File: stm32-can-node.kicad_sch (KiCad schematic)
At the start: 41 parts, among them J1 Conn_01x04_Pin, J2 Conn_01x10_Pin, J3 Conn_01x10_Pin, J4 Conn_01x05_Pin, U1 DS2484R_T, U2 R-783.3-0.5, U3 STM32U535CETx, U4 SN65HVD234, Y1 16MHz

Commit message: better pcb layout
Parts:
- added C16: 100n, Capacitor_SMD:C_0402_1005Metric, symbol Device:C
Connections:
- net +3.3V: now also C16.1
- net GND: now also C16.2
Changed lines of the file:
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@@
 	)
 	(junction
+		(at 156.21 157.48)
+		(diameter 0)
+		(color 0 0 0 0)
+	)
+	(junction
 		(at 232.41 26.67)
 		(diameter 0)
@@
 	(wire
 		(pts
+			(xy 68.58 33.02) (xy 68.58 36.83)
+		)
+		(stroke
+			(width 0)
+			(type default)
+		)
+	)
+	(wire
+		(pts
 			(xy 20.32 67.31) (xy 20.32 60.96)
 		)
@@
 	(wire
 		(pts
+			(xy 55.88 33.02) (xy 68.58 33.02)
+		)
+		(stroke
+			(width 0)
+			(type default)
+		)
+	)
+	(wire
+		(pts
 			(xy 68.58 44.45) (xy 68.58 46.99)
 		)
@@
 	(wire
 		(pts
-			(xy 55.88 33.02) (xy 68.58 33.02)
-		)
-		(stroke
-			(width 0)
-			(type default)
-		)
-	)
-	(wire
-		(pts
 			(xy 101.6 166.37) (xy 101.6 167.64)
 		)
@@
 	(wire
 		(pts
-			(xy 68.58 33.02) (xy 68.58 36.83)
+			(xy 68.58 25.4) (xy 68.58 33.02)
 		)
 		(stroke
@@
 	(wire
 		(pts
-			(xy 68.58 25.4) (xy 68.58 33.02)
-		)
-		(stroke
-			(width 0)
-			(type default)
-		)
-	)
-	(wire
-		(pts
 			(xy 247.65 59.69) (xy 254 59.69)
 		)
@@
 	)
 	(symbol
+		(lib_id "Device:C")
+		(at 156.21 161.29 0)
+		(unit 1)
+		(exclude_from_sim no)
+		(in_bom yes)
+		(on_board yes)
+		(dnp no)
+		(fields_autoplaced yes)
+		(property "Reference" "C16"
+			(at 160.02 160.02 0)
+			(effects
+				(font
+					(size 1.27 1.27)
+				)
+				(justify left)
+			)
+		)
+		(property "Value" "100n"
+			(at 160.02 162.56 0)
+			(effects
+				(font
+					(size 1.27 1.27)
+				)
+				(justify left)
+			)
+		)
+		(property "Footprint" "Capacitor_SMD:C_0402_1005Metric"
+			(at 157.1752 165.1 0)
+			(effects
+				(font
+					(size 1.27 1.27)
+				)
+				(hide yes)
+			)
+		)
+		(property "Datasheet" "~"
+			(at 156.21 161.29 0)
+			(effects
+				(font
+					(size 1.27 1.27)
+				)
+				(hide yes)
+			)
+		)
+		(property "Description" ""
+			(at 156.21 161.29 0)
+			(effects
+				(font
+					(size 1.27 1.27)
+				)
+			)
+		)
+		(pin "2"
+		)
+		(pin "1"
+		)
+		(instances
+			(project "stm32-can-node"
+				(path "/49496df6-b10b-410e-9292-bf7fa18df797"
+					(reference "C16")
+					(unit 1)
+				)
+			)
+		)
+	)
+	(symbol
 		(lib_name "+3.3V_2")
 		(lib_id "power:+3.3V")
@@
 					(unit 1)
 				)
+			)
+		)
+	)
+	(symbol
+		(lib_name "GND_1")
+		(lib_id "power:GND")
+		(at 156.21 165.1 0)
+		(unit 1)
+		(exclude_from_sim no)
+		(in_bom yes)
+		(on_board yes)
+		(dnp no)
+		(fields_autoplaced yes)
+		(property "Reference" "#PWR041"
+			(at 156.21 171.45 0)
+			(effects
+				(font
+					(size 1.27 1.27)
+				)
+				(hide yes)
+			)
+		)
+		(property "Value" "GND"
+			(at 156.21 170.18 0)
+			(effects
+				(font
+					(size 1.27 1.27)
+				)
+			)
+		)
+		(property "Footprint" ""
+			(at 156.21 165.1 0)
+			(effects
+				(font
+					(size 1.27 1.27)
+				)
+				(hide yes)
+			)
+		)
+		(property "Datasheet" ""
+			(at 156.21 165.1 0)
+			(effects
+				(font
+					(size 1.27 1.27)
+				)
+				(hide yes)
+			)
+		)
+		(property "Description" "Power symbol creates a global label with name \"GND\" , ground"
+			(at 156.21 165.1 0)
+			(effects
+				(font
+					(size 1.27 1.27)
+				)
+				(hide yes)
+			)
+		)
+		(pin "1"
+		)
+		(instances
+			(project "stm32-can-node"
+				(path "/49496df6-b10b-410e-9292-bf7fa18df797"
+					(reference "#PWR041")
+					(unit 1)
+				)

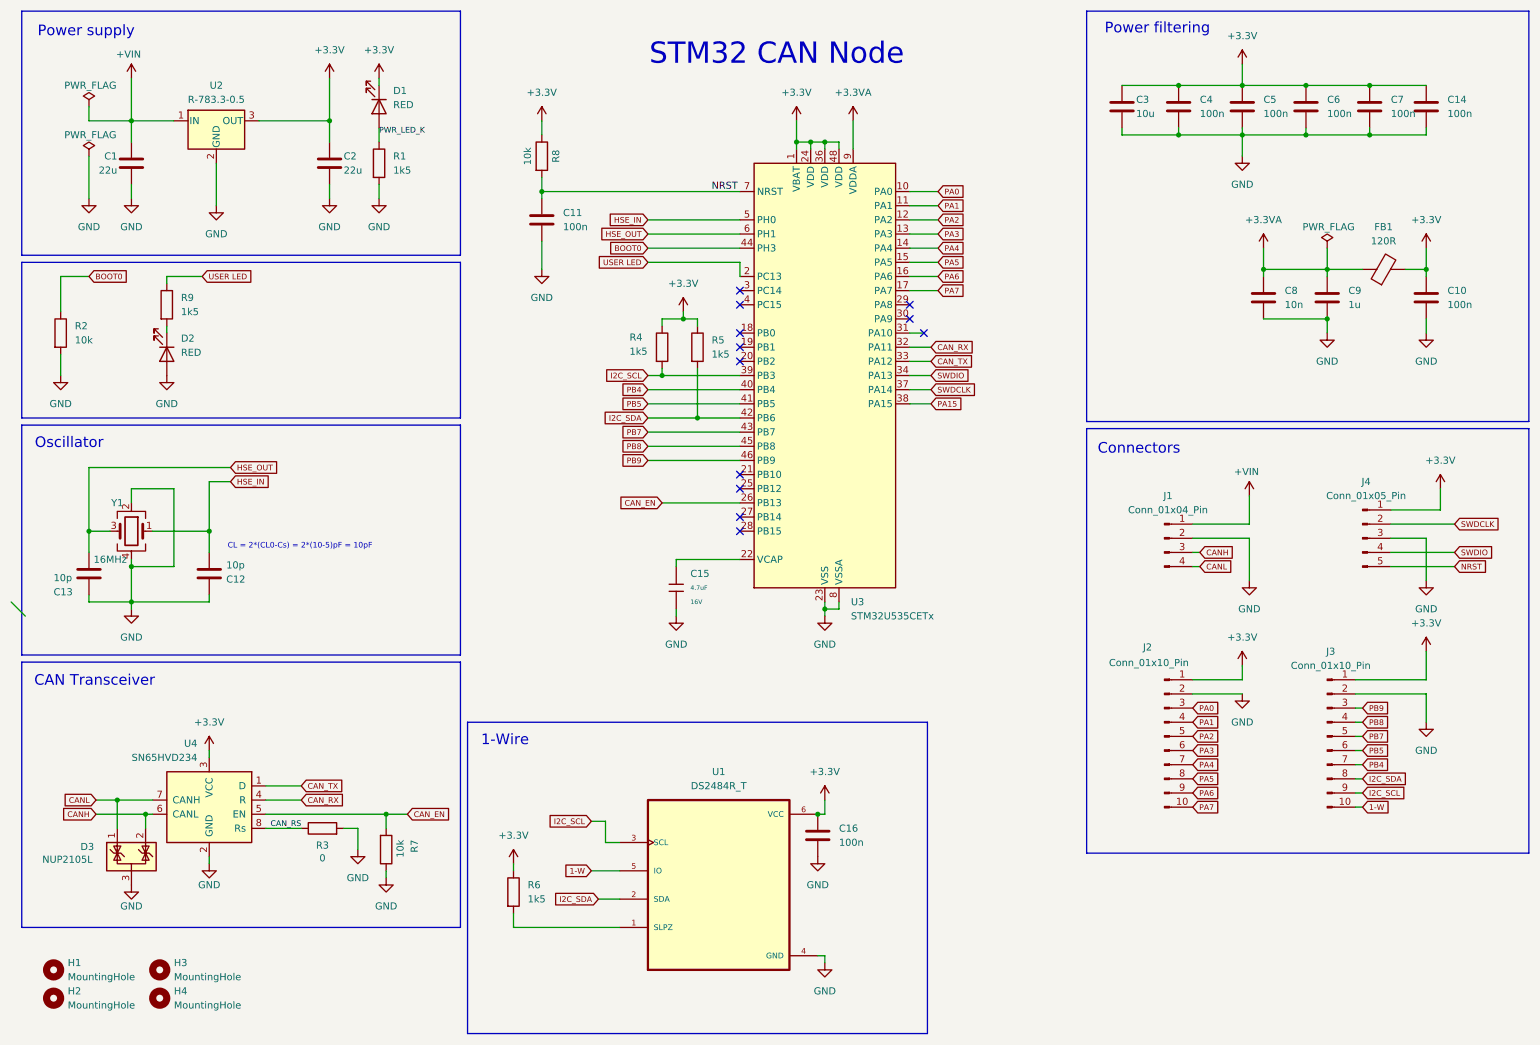
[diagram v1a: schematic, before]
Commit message: change to 11-pin connectors
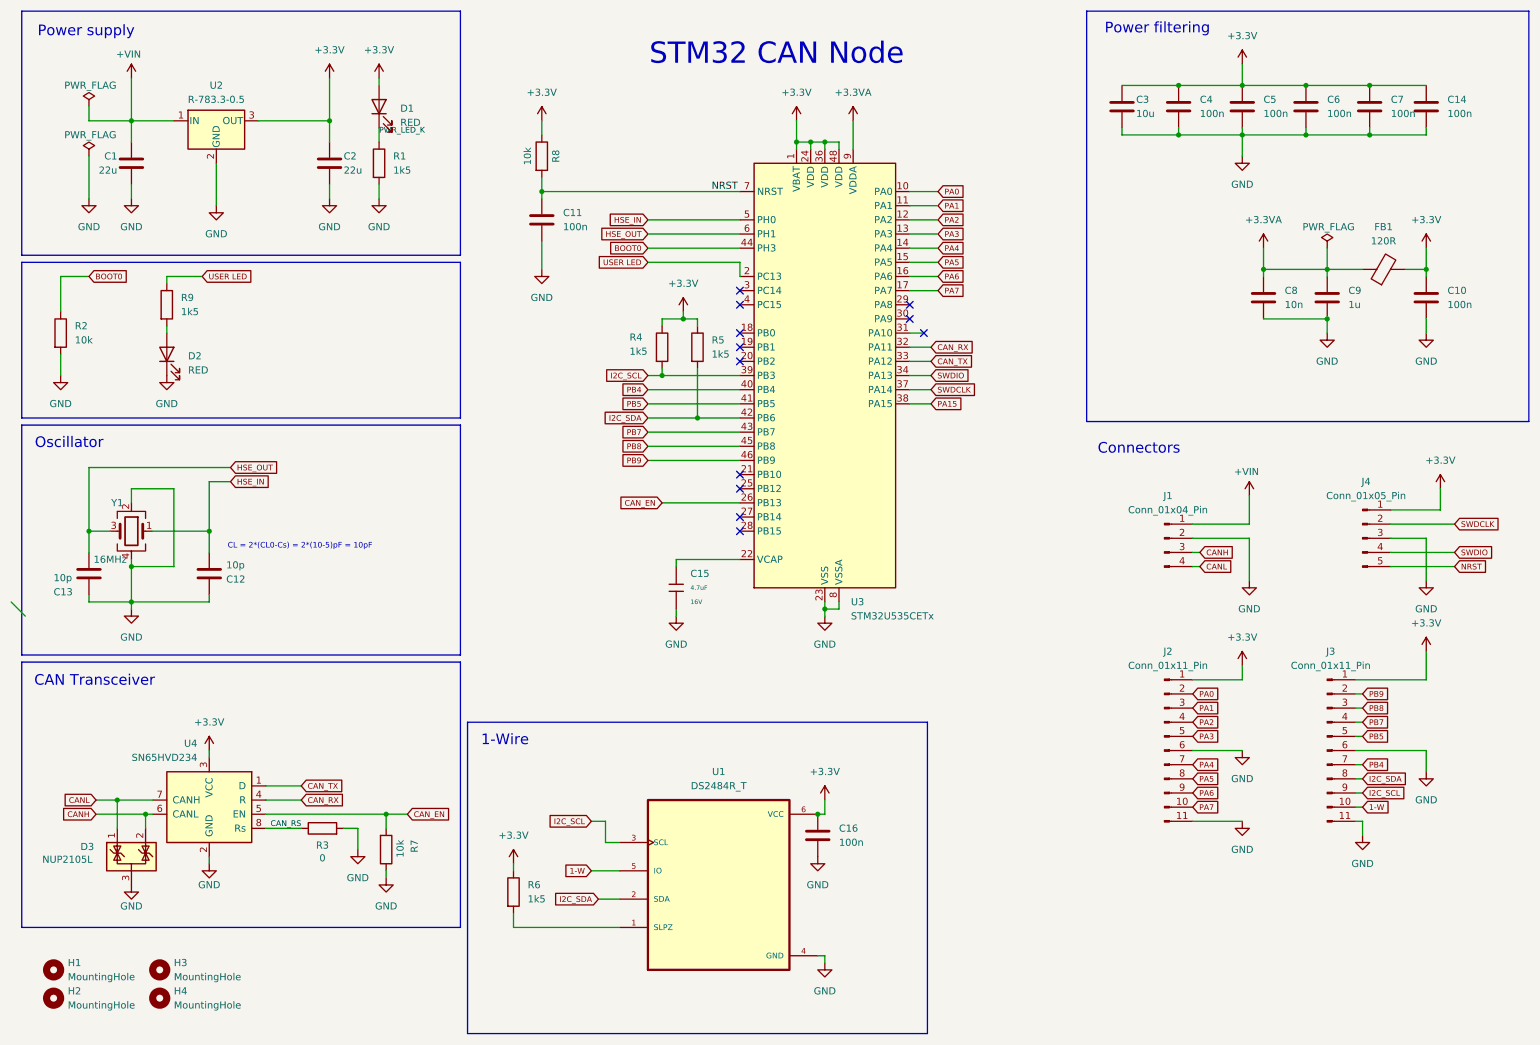
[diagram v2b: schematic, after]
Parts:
- removed J2, J3: Conn_01x10_Pin, Connector_PinHeader_2.54mm:PinHeader_1x10_P2.54mm_Vertical, symbol Connector:Conn_01x10_Pin
- added J2, J3: Conn_01x11_Pin, Connector_PinHeader_2.54mm:PinHeader_1x11_P2.54mm_Vertical, symbol Connector:Conn_01x11_Pin
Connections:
- net +3.3V: now also D1.2 (A), J2.1 (Pin_1), J3.1 (Pin_1); no longer D1.1 (K)
- net 1-W: now also J3.10 (Pin_10)
- net GND: now also D2.1 (K), J2.11 (Pin_11), J2.6 (Pin_6), J3.11 (Pin_11), J3.6 (Pin_6); no longer D2.2 (A)
- net I2C_SCL: now also J3.9 (Pin_9)
- net I2C_SDA: now also J3.8 (Pin_8)
- net PA0: now also J2.2 (Pin_2)
- net PA1: now also J2.3 (Pin_3)
- net PA2: now also J2.4 (Pin_4)
- net PA3: now also J2.5 (Pin_5)
- net PA4: now also J2.7 (Pin_7)
- net PA5: now also J2.8 (Pin_8)
- net PA6: now also J2.9 (Pin_9)
- net PA7: now also J2.10 (Pin_10)
- net PB4: now also J3.7 (Pin_7)
- net PB5: now also J3.5 (Pin_5)
- net PB7: now also J3.4 (Pin_4)
- net PB8: now also J3.3 (Pin_3)
- net PB9: now also J3.2 (Pin_2)
- net PWR_LED_K: now also D1.1 (K); no longer D1.2 (A)
- net at R9.2: now also D2.2 (A); no longer D2.1 (K)
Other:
- moved on the sheet: D1, D2

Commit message: add step-down converter, update part values
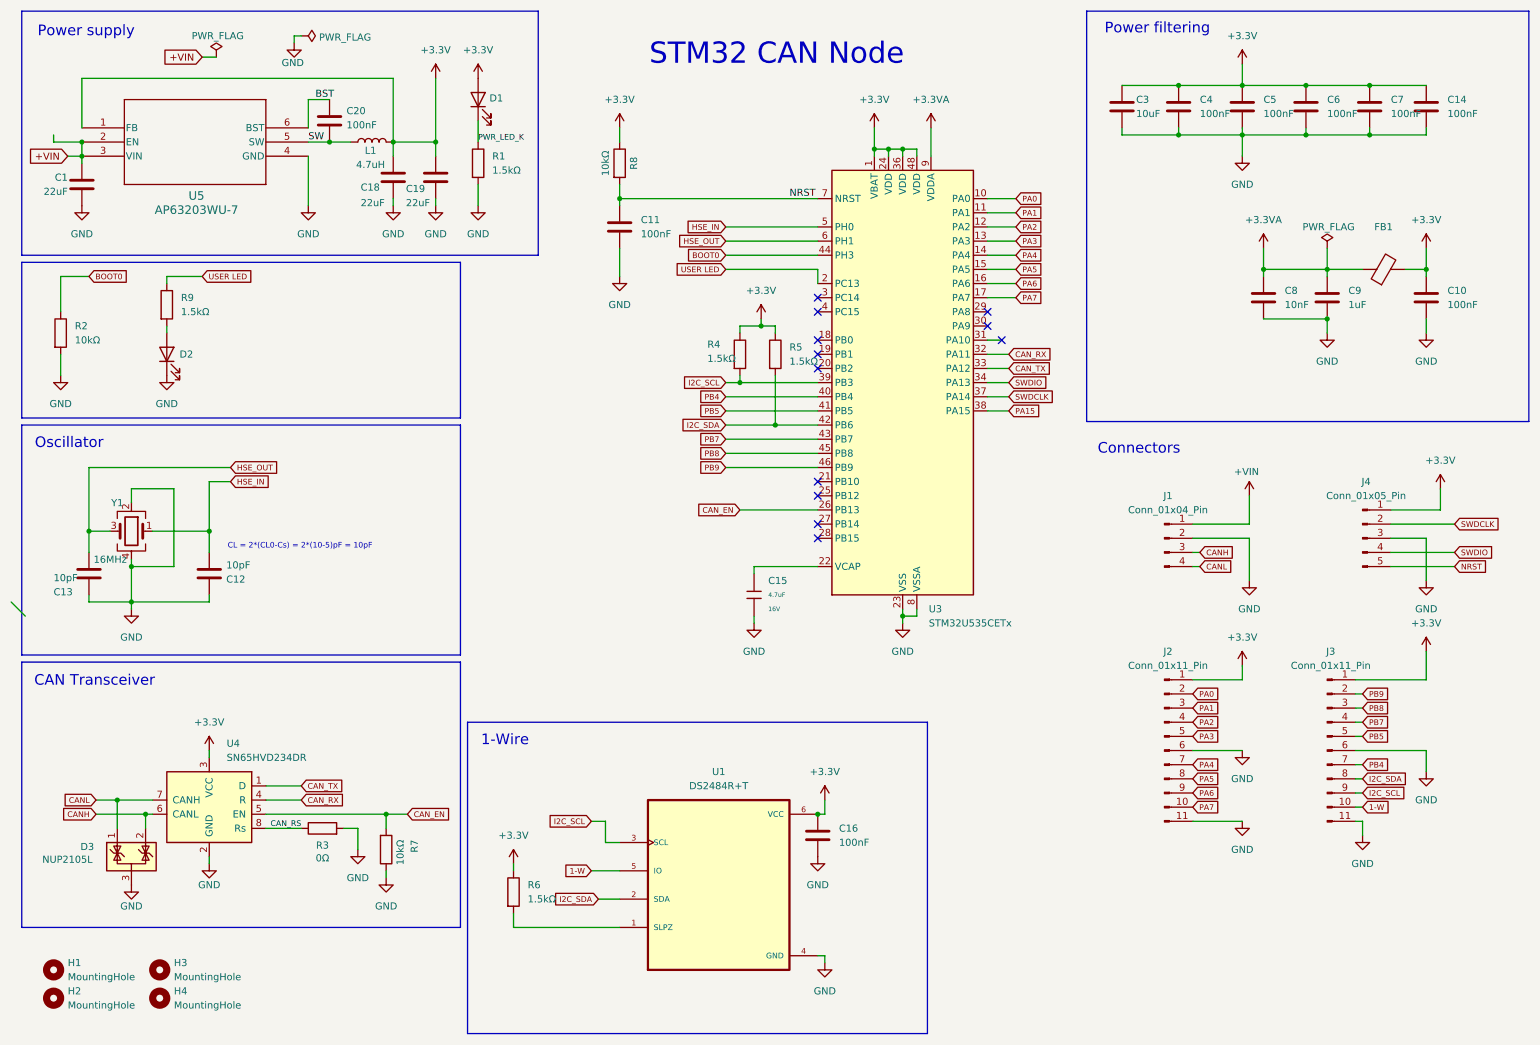
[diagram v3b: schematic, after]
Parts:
- removed C2: 22u, Capacitor_SMD:C_0805_2012Metric, symbol Device:C
- removed U2: R-783.3-0.5, mrk:CONV_R-783.3-0.5, symbol Regulator_Switching:R-783.3-0.5
- added C18, C19: 22uF, Capacitor_SMD:C_0603_1608Metric, symbol Device:C
- added C20: 100nF, Capacitor_SMD:C_0402_1005Metric, symbol Device:C
- added L1: 4.7uH, Inductor_SMD_Wurth:L_Wurth_WE-LQSH-4020, symbol Device:L
- added U5: AP63203WU-7, footprints:AP63203WU-7_DIO, symbol ap63203:AP63203WU-7
- C1: value 22u -> 22uF
- C10, C11, C14, C16, C4, C5, C6, C7: value 100n -> 100nF
- C12, C13: value 10p -> 10pF
- C15: footprint PCM_JLCPCB:C_0603 -> Capacitor_SMD:C_0603_1608Metric
- C3: value 10u -> 10uF
- C8: value 10n -> 10nF
- C9: value 1u -> 1uF
- D1: value RED -> C397045
- D2: value RED -> C165977
- FB1: value 120R -> FCM1608KF-601T05; footprint Inductor_SMD:L_0603_1608Metric -> Inductor_SMD:L_0805_2012Metric
- R1, R4, R5, R6, R9: value 1k5 -> 1.5kΩ
- R2, R7, R8: value 10k -> 10kΩ
- R3: value 0 -> 0Ω; footprint PCM_JLCPCB:R_0402 -> Resistor_SMD:R_0402_1005Metric
- U1: value DS2484R_T -> DS2484R+T
- U3: footprint Package_QFP:LQFP-48_7x7mm_P0.5mm -> Package_DFN_QFN:QFN-48-1EP_7x7mm_P0.5mm_EP5.6x5.6mm
- U4: value SN65HVD234 -> SN65HVD234DR
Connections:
- net +3.3V: now also C18.1, C19.1, L1.2, U5.1 (FB)
- net +VIN: now also U5.2 (EN), U5.3 (VIN)
- net GND: now also C18.2, C19.2, U5.4 (GND)
- new net BST: C20.1, U5.6 (BST)
- new net SW: C20.2, L1.1, U5.5 (SW)
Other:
- moved on the sheet: C1, C11, C15, D1, R1, R4, R5, R8, U3

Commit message: support for UFQFPN48_SMPS
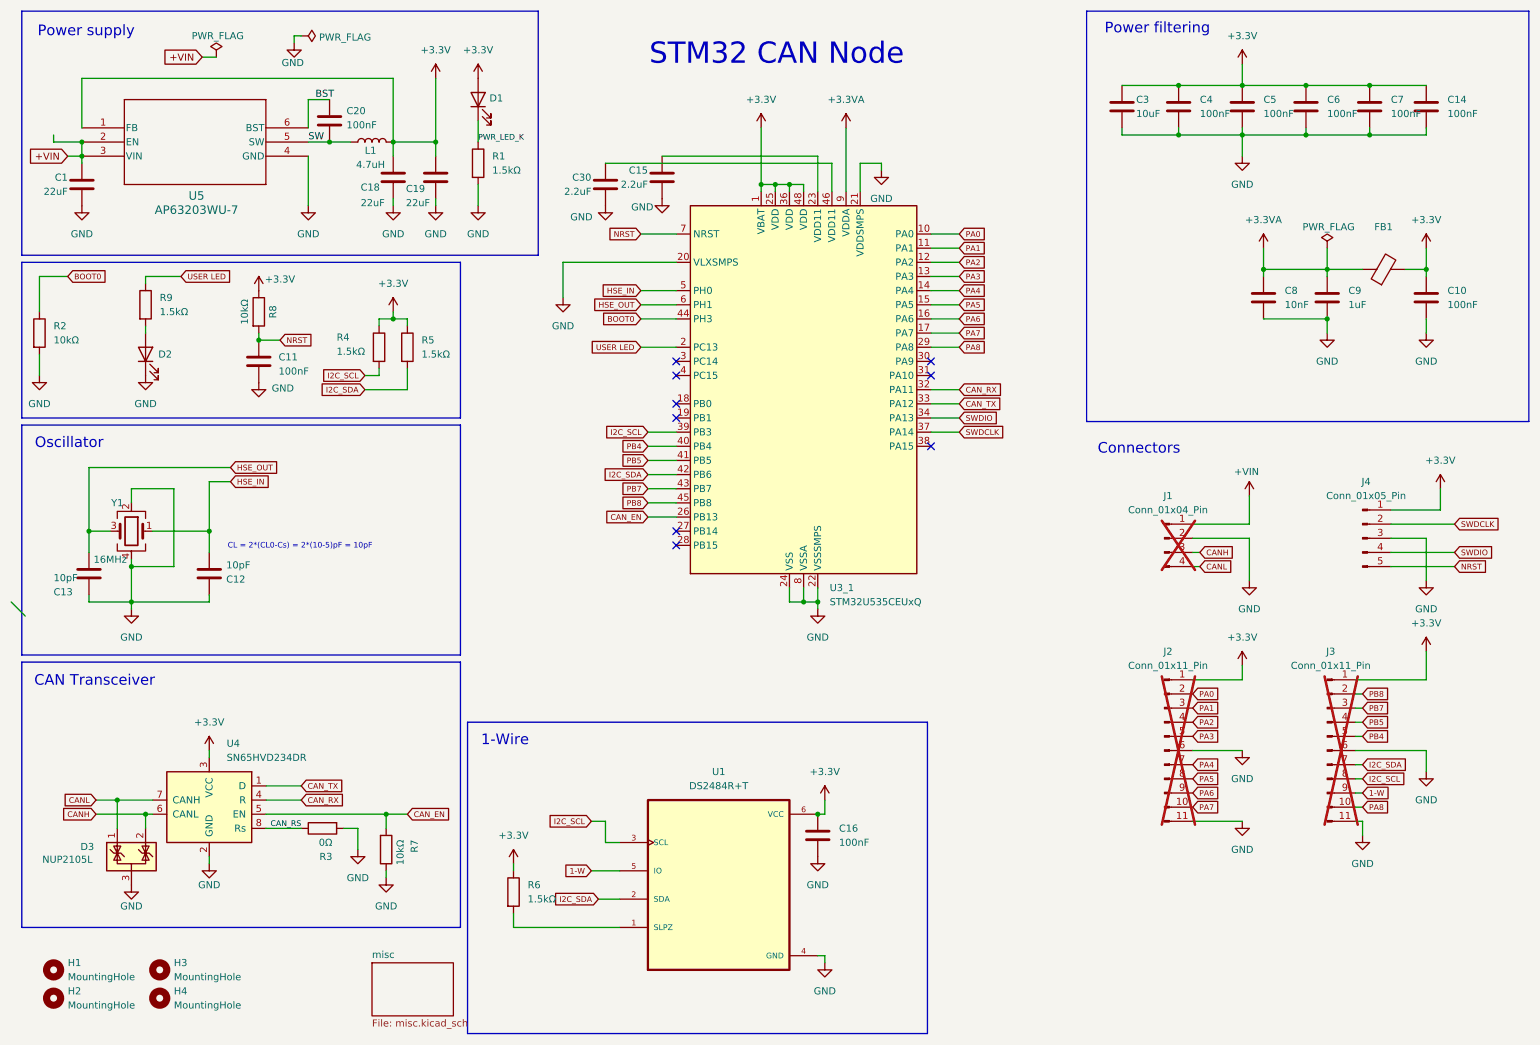
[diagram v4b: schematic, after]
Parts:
- removed C15: 4.7uF, Capacitor_SMD:C_0603_1608Metric, symbol PCM_JLCPCB-Capacitors:0603,4.7uF
- removed R3: 0Ω, Resistor_SMD:R_0402_1005Metric, symbol PCM_JLCPCB-Resistors:0402,10kΩ
- removed U3: STM32U535CETx, Package_DFN_QFN:QFN-48-1EP_7x7mm_P0.5mm_EP5.6x5.6mm, symbol MCU_ST_STM32U5:STM32U535CETx
- added C15, C30: 2.2uF, Capacitor_SMD:C_0603_1608Metric, symbol Device:C
- added R3: 0Ω, Resistor_SMD:R_0402_1005Metric, symbol Device:R
- added U3_1: STM32U535CEUxQ, Package_DFN_QFN:QFN-48-1EP_7x7mm_P0.5mm_EP5.6x5.6mm, symbol MCU_ST_STM32U5:STM32U535CEUxQ
- FB1: footprint Inductor_SMD:L_0805_2012Metric -> Inductor_SMD:L_0603_1608Metric; JLC (none) -> C133937
- J1, J2, J3: now not fitted; now left out of the parts list
- J4: JLC (none) -> C2935945; RotOffset (none) -> -90
- L1: footprint Inductor_SMD_Wurth:L_Wurth_WE-LQSH-4020 -> mrk:IND_SRP4020TA-4R7M
- U1: JLC (none) -> C124886; RotOffset (none) -> -90
- U4: JLC (none) -> C99818
- U5: JLC (none) -> C780769; RotOffset (none) -> -90
- Y1: JLC (none) -> C13738
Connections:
- net PB9 is gone; now on net PB8: J3.2 (Pin_2)
- net +3.3V: now also U3_1.1 (VBAT), U3_1.25 (VDD), U3_1.36 (VDD), U3_1.48 (VDD)
- net +3.3VA: now also U3_1.9 (VDDA)
- net 1-W: now also J3.9 (Pin_9); no longer J3.10 (Pin_10)
- net BOOT0: now also U3_1.44 (PH3)
- net CAN_EN: now also U3_1.26 (PB13)
- net CAN_RS: now also R3.1
- net CAN_RX: now also U3_1.32 (PA11)
- net CAN_TX: now also U3_1.33 (PA12)
- net GND: now also C15.2, C30.2, R3.2, U3_1.20 (VLXSMPS), U3_1.21 (VDDSMPS), U3_1.22 (VSSSMPS), U3_1.24 (VSS), U3_1.35 (VSS), U3_1.47 (VSS), U3_1.49 (VSS), U3_1.8 (VSSA)
- net HSE_IN: now also U3_1.5 (PH0)
- net HSE_OUT: now also U3_1.6 (PH1)
- net I2C_SCL: now also J3.8 (Pin_8), U3_1.39 (PB3); no longer J3.9 (Pin_9)
- net I2C_SDA: now also J3.7 (Pin_7), U3_1.42 (PB6); no longer J3.8 (Pin_8)
- net NRST: now also U3_1.7 (NRST)
- net PA0: now also U3_1.10 (PA0)
- net PA1: now also U3_1.11 (PA1)
- net PA2: now also U3_1.12 (PA2)
- net PA3: now also U3_1.13 (PA3)
- net PA4: now also U3_1.14 (PA4)
- net PA5: now also U3_1.15 (PA5)
- net PA6: now also U3_1.16 (PA6)
- net PA7: now also U3_1.17 (PA7)
- net PB4: now also J3.5 (Pin_5), U3_1.40 (PB4); no longer J3.7 (Pin_7)
- net PB5: now also J3.4 (Pin_4), U3_1.41 (PB5); no longer J3.5 (Pin_5)
- net PB7: now also J3.3 (Pin_3), U3_1.43 (PB7); no longer J3.4 (Pin_4)
- net PB8: now also U3_1.45 (PB8); no longer J3.3 (Pin_3)
- net SWDCLK: now also U3_1.37 (PA14)
- net SWDIO: now also U3_1.34 (PA13)
- net USER LED: now also U3_1.2 (PC13)
- new net: C15.1, U3_1.23 (VDD11)
- new net: C30.1, U3_1.46 (VDD11)
- new net PA8: J3.10 (Pin_10), U3_1.29 (PA8)
- no-connect marks 12 -> 9
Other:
- added sheet misc (misc.kicad_sch)
- moved on the sheet: C11, D2, R2, R4, R5, R8, R9

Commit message: update images
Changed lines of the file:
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@@
 	)
 	(sheet
-		(at 76.2 184.15)
+		(at 61.595 183.515)
 		(size 14.605 9.525)
 		(exclude_from_sim no)
@@
 		)
 		(property "Sheetname" "misc"
-			(at 76.2 183.4384 0)
+			(at 61.595 182.8034 0)
 			(effects
 				(font
@@
 		)
 		(property "Sheetfile" "misc.kicad_sch"
-			(at 76.2 194.2596 0)
+			(at 61.595 193.6246 0)
 			(effects
 				(font
